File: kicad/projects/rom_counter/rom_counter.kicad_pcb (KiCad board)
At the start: 2 copper layers, 203.2 x 97.8 mm, 43 parts, among them J1 peripheral_addr_bus_connector, J2 peripheral_aux_connector, J3 peripheral_membank_connector, J4 Conn_02x16_Odd_Even, J5 Conn_01x16_Socket, J6 Conn_01x02_Socket, J7 Conn_01x02_Pin, J8 Conn_01x02_Socket, U1 28C256, U10 74HC161, U11 74HC245, U12 74HC245, U2 28C256, U3 74HC30, U4 74HC30, U5 74HC32, U6 74HC00, U7 74HC161, U8 74HC161, U9 74HC161

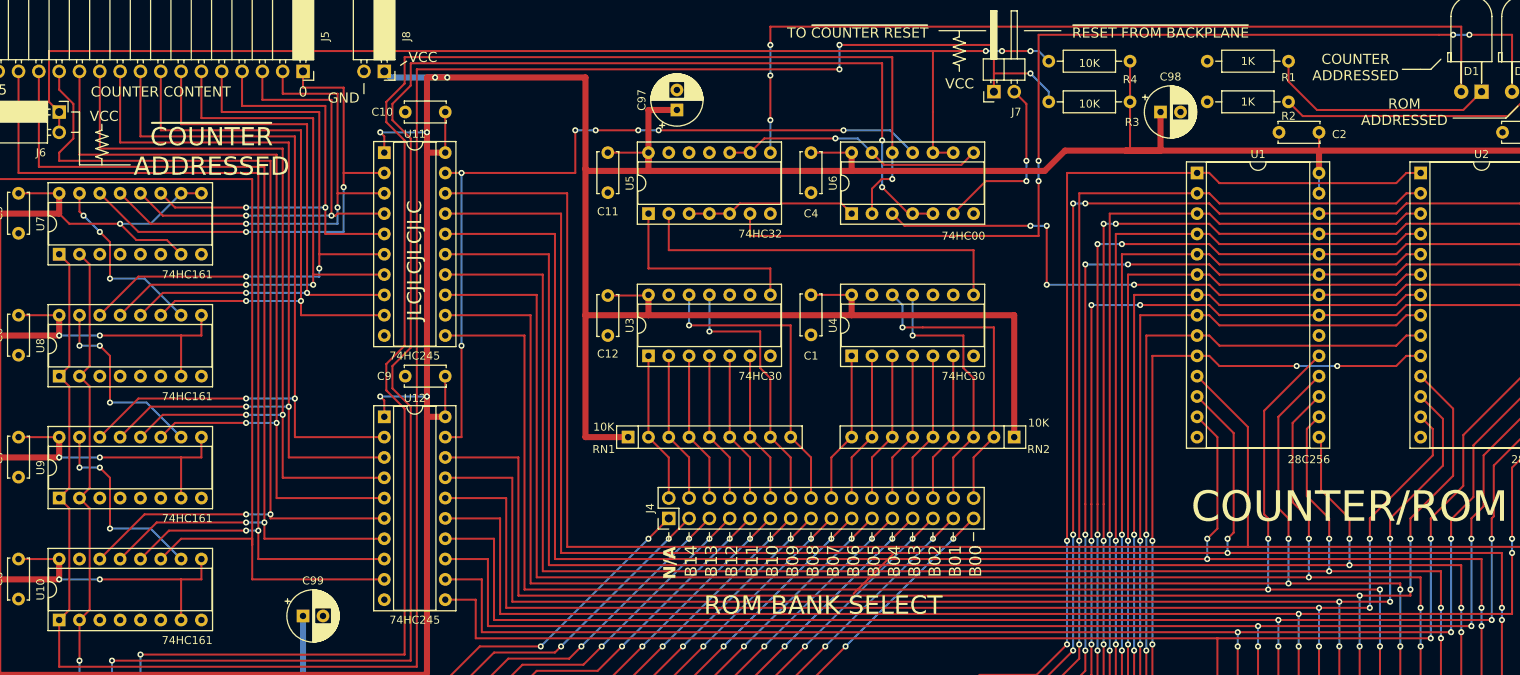
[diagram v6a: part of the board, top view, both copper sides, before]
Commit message: Un invert counter addressed. Almost done on peripheral connect PCB.
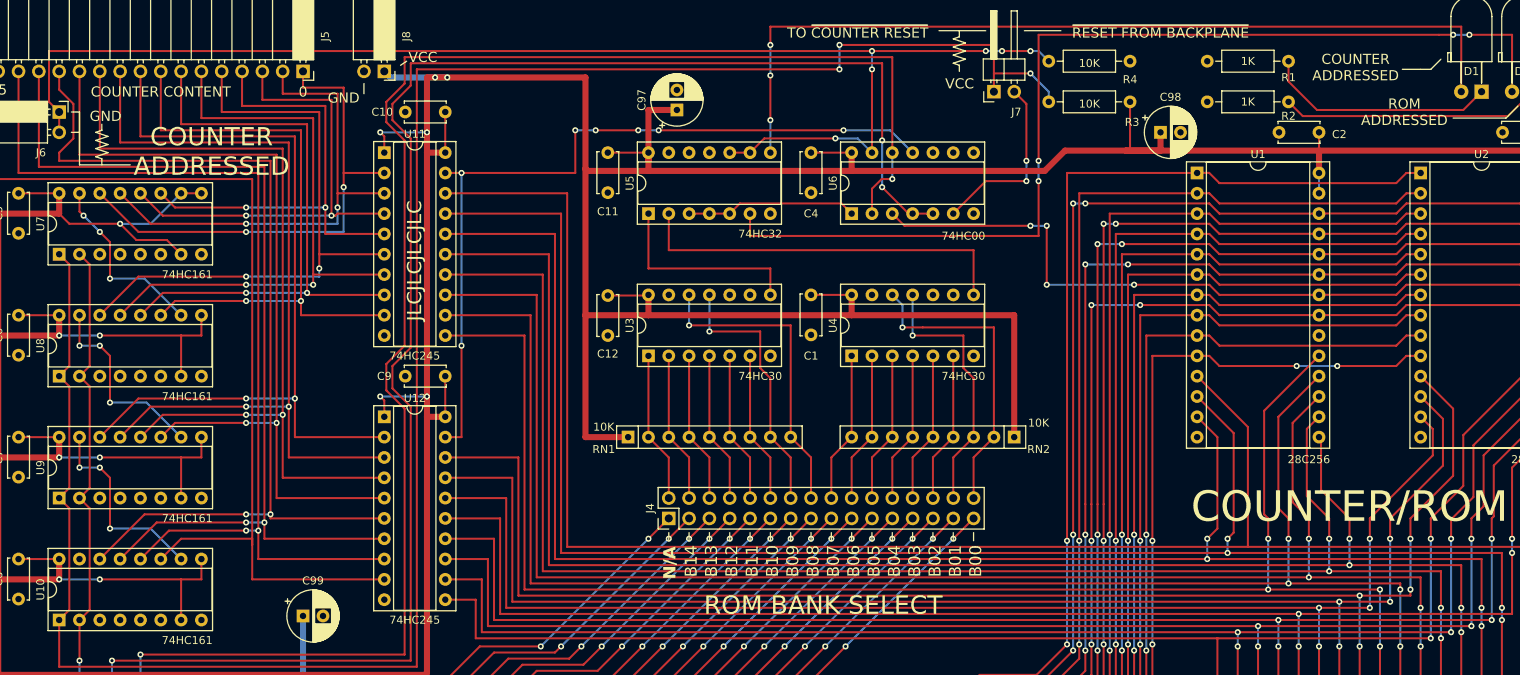
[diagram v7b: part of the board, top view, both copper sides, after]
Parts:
- moved C98 2.54 mm to (198.6, 68.6)
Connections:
- J6 pad 1: /~{COUNTER ADDRESSED} -> /COUNTER ADDRESSED
- J6 pad 2: /~{COUNTER ADDRESSED} -> /COUNTER ADDRESSED
- R4 pad 1: /~{COUNTER ADDRESSED} -> /COUNTER ADDRESSED
- R4 pad 2: VCC -> GND
- U6 pad 10: /~{COUNTER ADDRESSED} -> GND
- U6 pad 8: /COUNTER ADDRESSED -> unconnected-(U6-Pad8)
- U6 pad 9: /~{COUNTER ADDRESSED} -> GND
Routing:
- net /~{COUNTER ADDRESSED}: track 151.4 -> 0.00 mm, vias 3 -> 0
- net /COUNTER ADDRESSED: track 33.2 -> 168.1 mm, vias 1 -> 6
- net VCC: track 755.1 -> 747.5 mm
- net /BANK_BUS_06: track 54.3 -> 47.1 mm
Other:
- board text removed: "~{COUNTER} ADDRESSED"

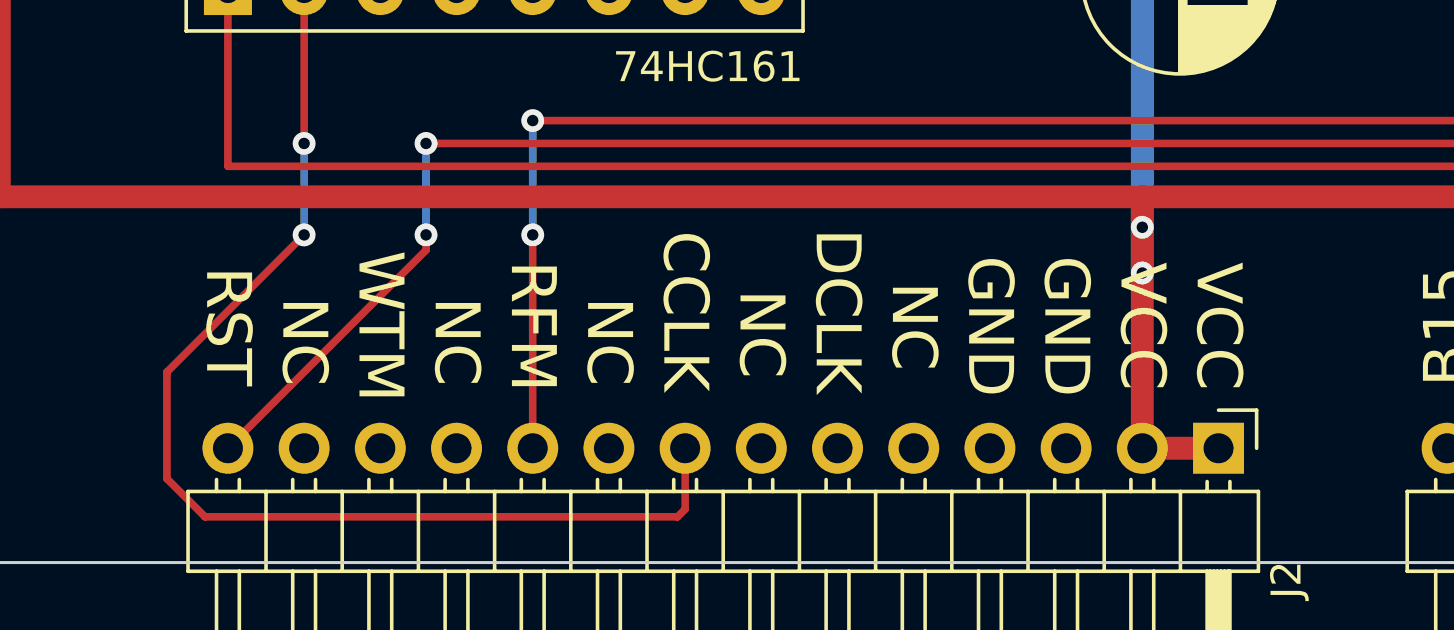
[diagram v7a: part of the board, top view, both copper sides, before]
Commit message: Tech check and exploration for single signal RAM direction.
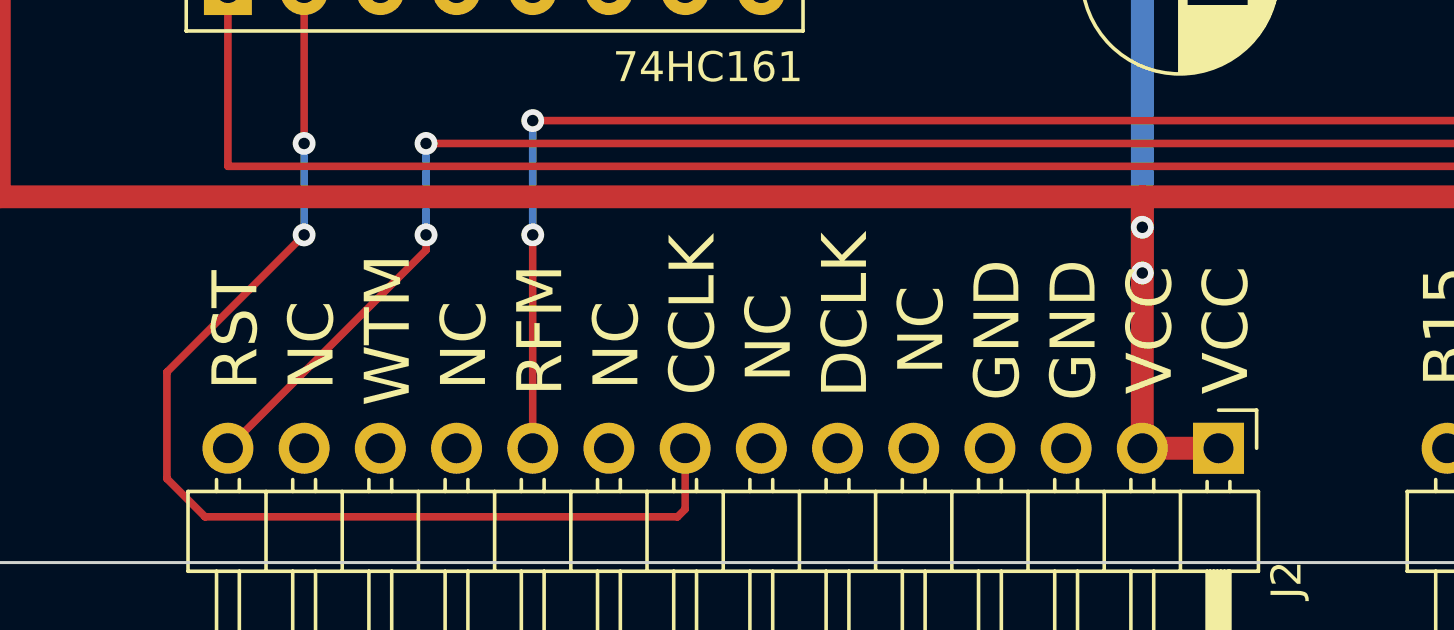
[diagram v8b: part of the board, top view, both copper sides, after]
